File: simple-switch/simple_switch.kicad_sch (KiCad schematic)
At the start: 21 parts, among them J1 CON_TERM_BLK_1X2_TB008A-508-0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, J2 CON_HDR_100MILS_M_TH_2X8, J3 CON_HDR_100MILS_M_TH_1X2, Q1 TRX_PMOS_AOD4189, Q2 TRX_2NPN_BC846S,115

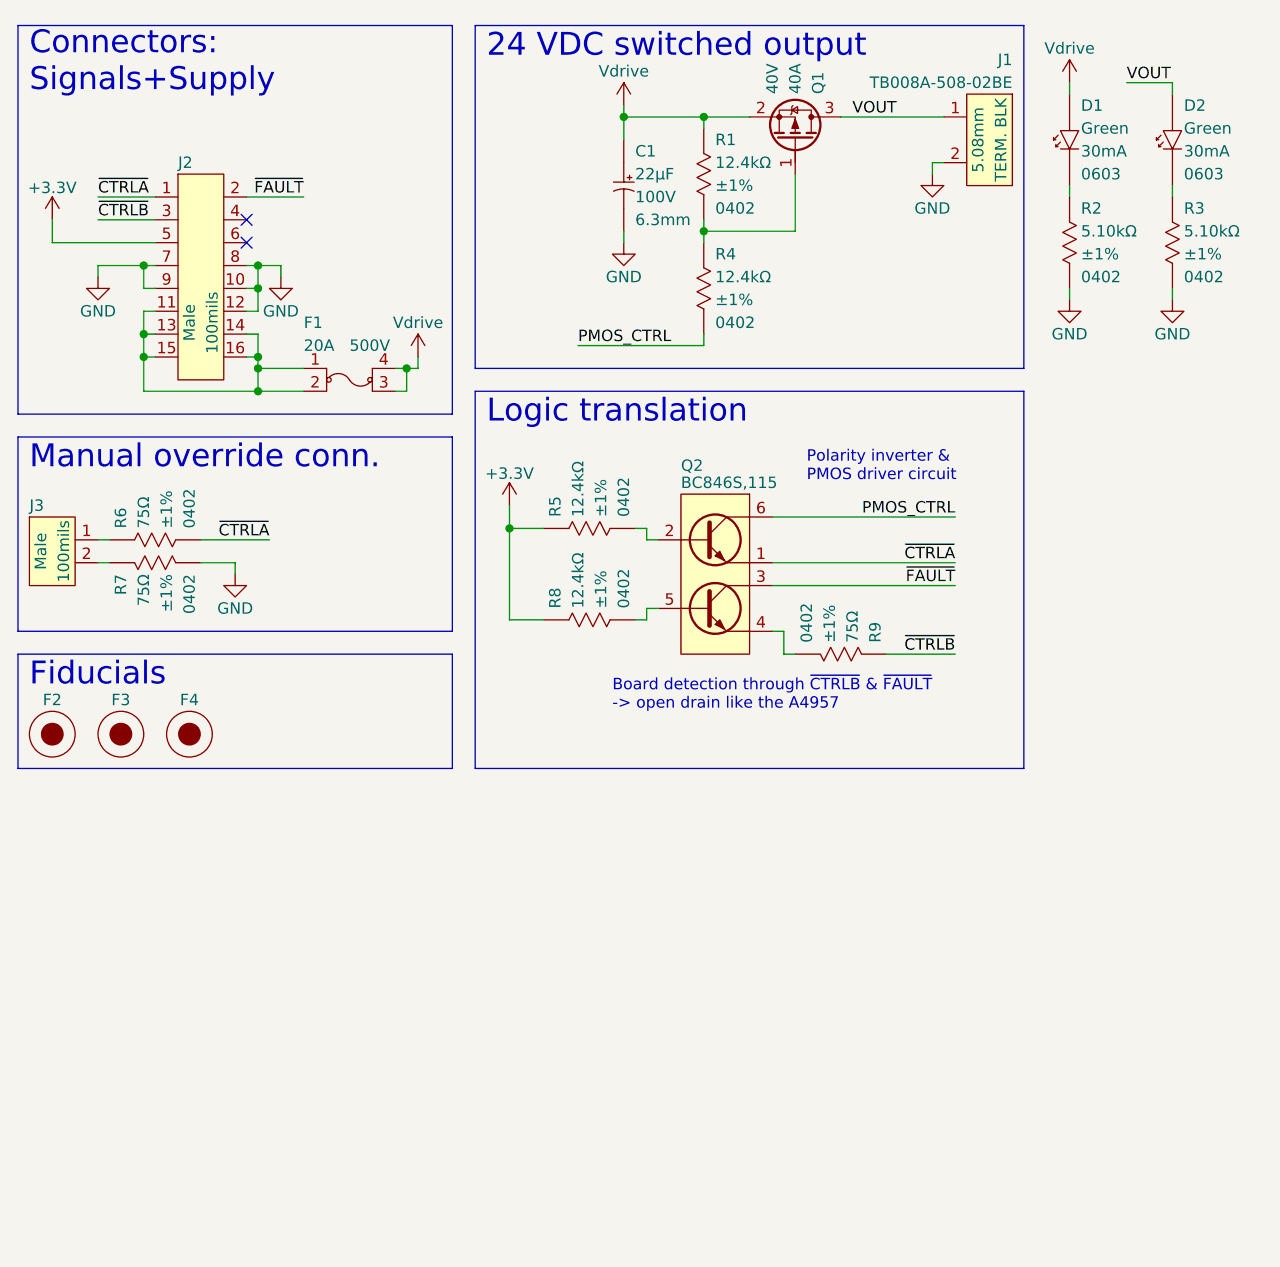
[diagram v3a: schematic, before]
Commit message: Invert connectors (male/female) Replace TH connectors with SMD ones on mainboard Add 555 timer on simple-switch to generate 60 Hz Add jumper on simple-switch to select AC Add series I2C resistors on mainboard from mikroBUS socket
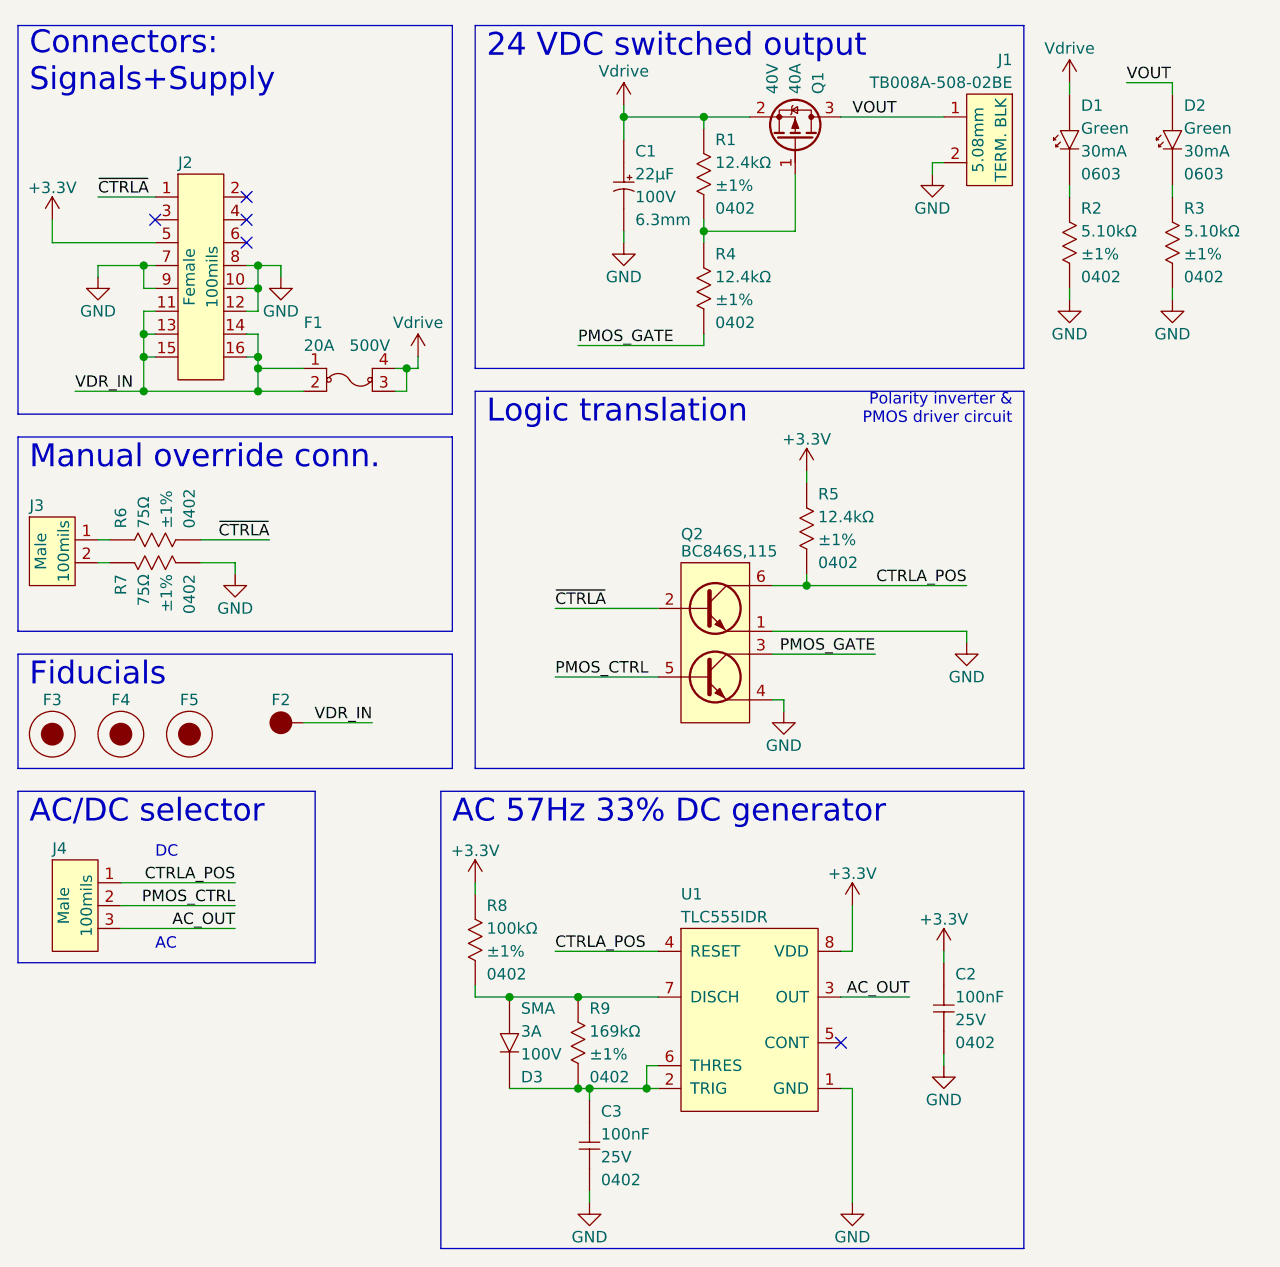
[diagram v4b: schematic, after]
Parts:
- removed J2: CON_HDR_100MILS_M_TH_2X8, connaxio-connectors:CON_HDR_100MILS_M_TH_2X8, symbol connaxio-connectors:CON_HDR_100MILS_M_TH_2X8
- removed R8: RES_12.4KΩ_1%_0402, connaxio-resistors:RES_0402_1005M, symbol connaxio-resistors:RES_12.4KΩ_1%_0402
- removed R9: RES_226Ω_1%_0402, connaxio-resistors:RES_0402_1005M, symbol connaxio-resistors:RES_75Ω_1%_0402
- added C2, C3: CAP_CER_100NF_25V_0402, connaxio-capacitors:CAP_CER_0402_1005M, symbol connaxio-capacitors:CAP_CER_100NF_25V_0402
- added D3: DIO_SBD_100V_3A_SMA, connaxio-diodes:DO-214AC_SMA, symbol connaxio-diodes:DIO_SBD_100V_3A_SMA
- added F2: FID_1X1, connaxio-mechanical:FID_1X1, symbol connaxio-mechanical:FID_1X1
- added J2: CON_HDR_100MILS_F_TH_2X8, connaxio-connectors:CON_HDR_100MILS_F_TH_2X8, symbol connaxio-connectors:CON_HDR_100MILS_F_TH_2X8
- added J4: CON_HDR_100MILS_M_TH_1X3, connaxio-connectors:CON_HDR_100MILS_M_TH_1X3, symbol connaxio-connectors:CON_HDR_100MILS_M_TH_1X3
- added R8: RES_100KΩ_1%_0402, connaxio-resistors:RES_0402_1005M, symbol connaxio-resistors:RES_100KΩ_1%_0402
- added R9: RES_169KΩ_1%_0402, connaxio-resistors:RES_0402_1005M, symbol connaxio-resistors:RES_169KΩ_1%_0402
- added U1: TIMER_TLC555IDR, connaxio-sop:SOIC-8_3.9x4.9_P1.27, symbol connaxio-ic:TIMER_TLC555IDR
- renumbered F2 to F3, F3 to F4, F4 to F5
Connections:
- net +3.3V: now also C2.1, J2.5, R8.1, U1.8 (VDD)
- net GND: now also Q2.1 (E1), Q2.4 (E2), C2.2, C3.2, J2.10, J2.12, J2.7, J2.8, J2.9, U1.1 (GND)
- net PMOS_CTRL: now also Q2.5 (B2), J4.2; no longer Q2.6 (C1), R4.2
- net ~{CTRLA}: now also Q2.2 (B1), J2.1; no longer Q2.1 (E1)
- net CTRLA_POS: now reaches R5.2
- net CTRLA_POS: now also Q2.6 (C1), J4.1, U1.4 (RESET); no longer Q2.2 (B1)
- net VDR_IN: now reaches F1.1, F1.2
- net VDR_IN: now also F2.1, J2.11, J2.13, J2.14, J2.15, J2.16
- net ~{FAULT} renamed PMOS_GATE
- net PMOS_GATE: now also R4.2
- new net: C3.1, D3.1 (K), R9.2, U1.2 (TRIG), U1.6 (THRES)
- new net: D3.2 (A), R8.2, R9.1, U1.7 (DISCH)
- new net AC_OUT: J4.3, U1.3 (OUT)
- no-connect marks 2 -> 5
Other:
- note added: "AC 57Hz 33% DC generator"
- note added: "AC/DC selector"
- note added: "DC AC"
- note removed: "Board detection through ~{CTRLB} & ~{FAULT} -> open drain like the A4957"
- moved on the sheet: Q2

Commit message: Add flyback diode to simple-switch
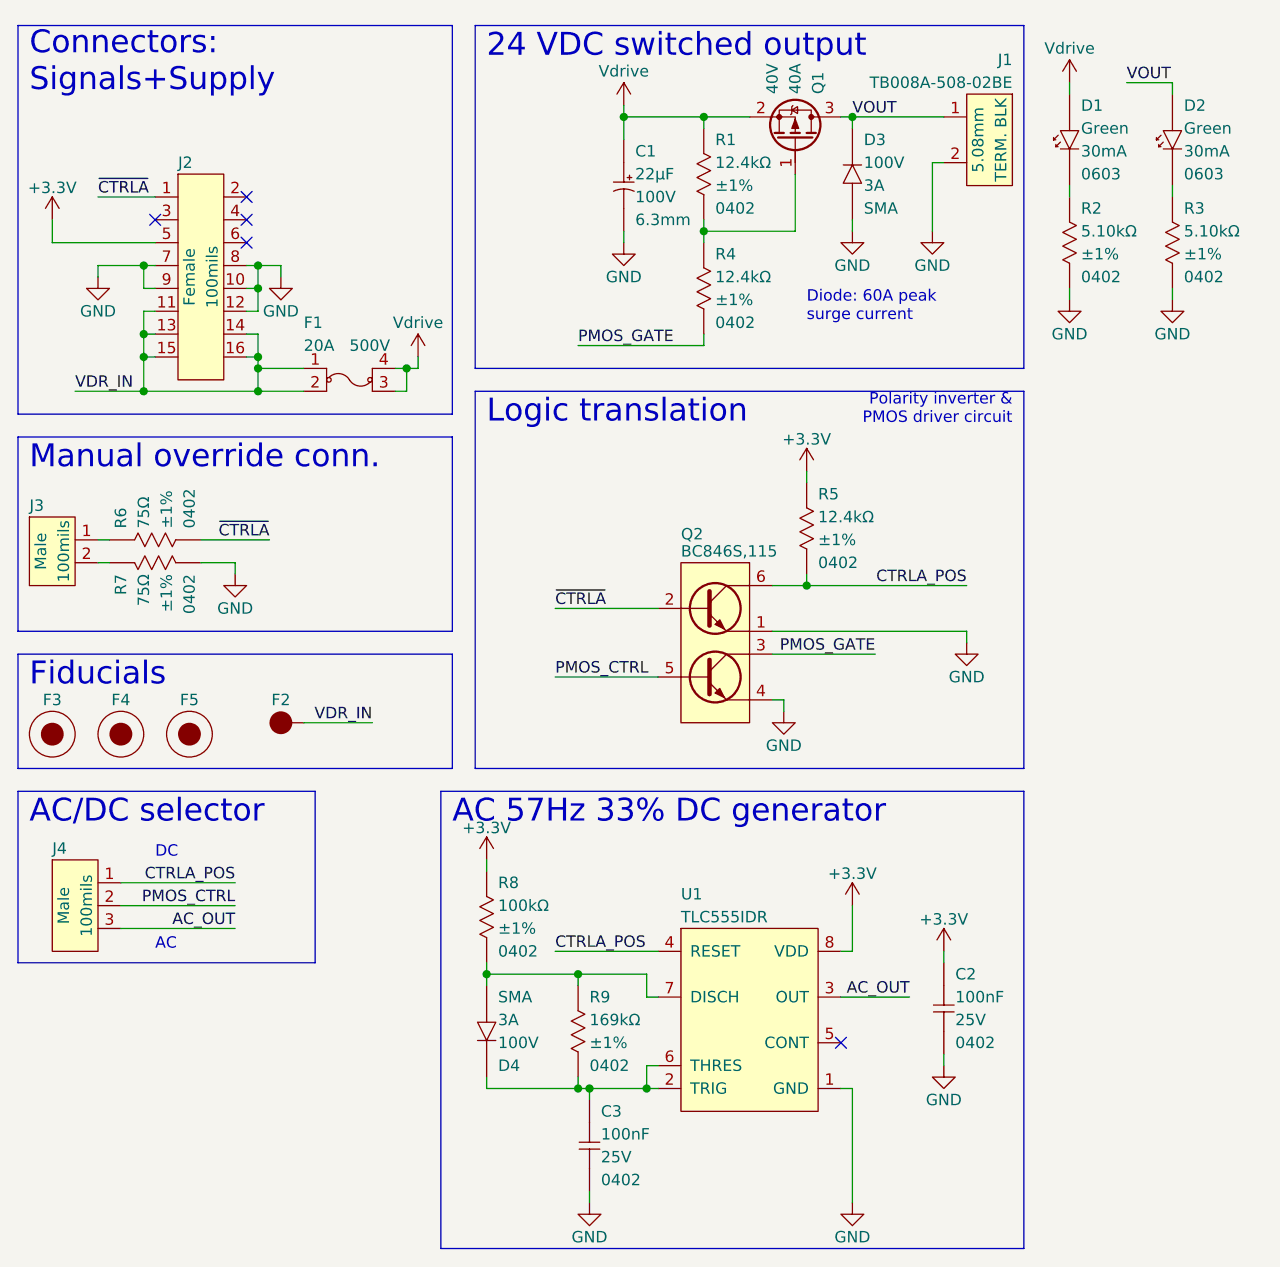
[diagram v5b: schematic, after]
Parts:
- added D3: DIO_SBD_100V_3A_SMA, connaxio-diodes:DO-214AC_SMA, symbol connaxio-diodes:DIO_SBD_100V_3A_SMA
- renumbered D3 to D4
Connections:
- net GND: now also D3.2 (A)
- net VOUT: now also D3.1 (K)
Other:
- note added: "Diode: 60A peak surge current"
- moved on the sheet: D4, R8, R9
